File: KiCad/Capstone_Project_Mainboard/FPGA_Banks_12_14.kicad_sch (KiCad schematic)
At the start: 2 parts, among them U1 XC7K160T-FFG676_MIB

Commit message: Updated FPGA Footprint
Added die-to-pad length offsets to all pins of the FFG676 package. These values were derived from the delay files provided in Vivado.
+ Other minor bugfixes
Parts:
- U1: footprint Capstone_Library:Xilinx_FFG676_MOD -> Capstone_Library:Xilinx_FFG676_K7_160T
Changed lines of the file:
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@@
   (title_block
     (title "FPGA Banks 12 & 14 I/O")
-    (date "2023-12-18")
+    (date "2023-12-22")
     (rev "A")
     (company "Jordan Harris-Toovy")
@@
       (effects (font (size 1.27 1.27)) (justify right))
     )
-    (property "Footprint" "Capstone_Library:Xilinx_FFG676_MOD" (at 73.66 20.32 0)
+    (property "Footprint" "Capstone_Library:Xilinx_FFG676_K7_160T" (at 73.66 20.32 0)
       (effects (font (size 1.27 1.27)) hide)
     )
@@
       (effects (font (size 1.27 1.27)) (justify right))
     )
-    (property "Footprint" "Capstone_Library:Xilinx_FFG676_MOD" (at 185.42 20.32 0)
-      (effects (font (size 1.27 1.27)) hide)
-    )
+    (property "Footprint" "Capstone_Library:Xilinx_FFG676_K7_160T" (at 185.42 20.32 0)
+      (effects (font (size 1.27 1.27)) hide)
+    )

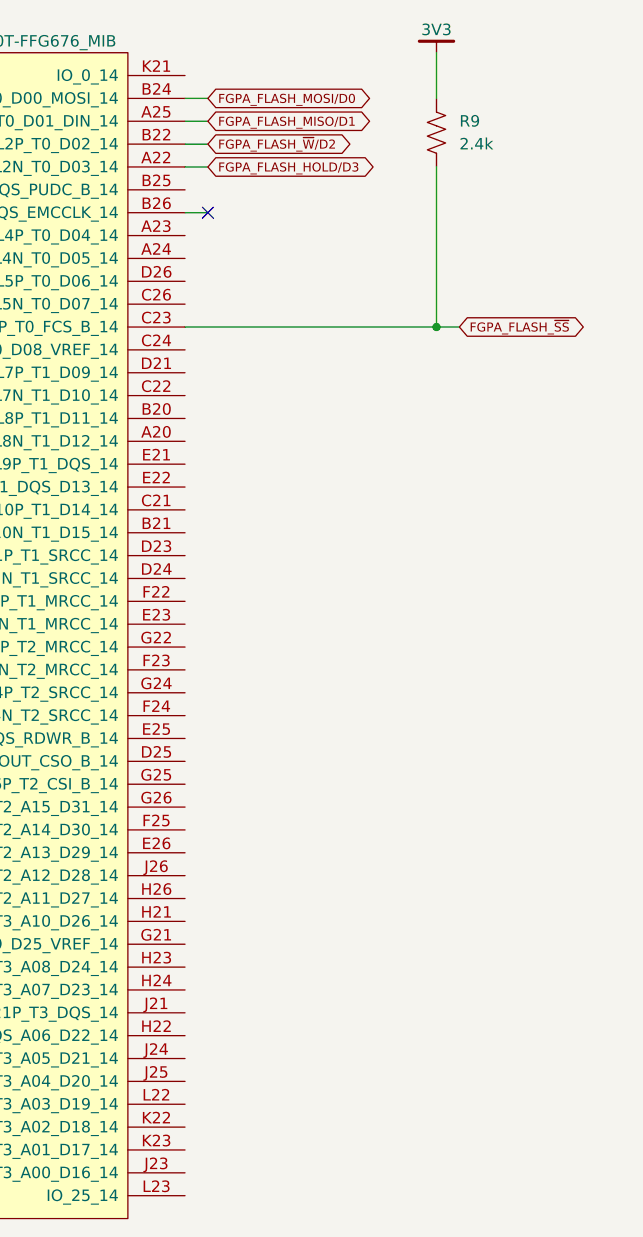
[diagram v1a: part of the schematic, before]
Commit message: Core non-power parts defined
Most major non-power components added to KiCad project
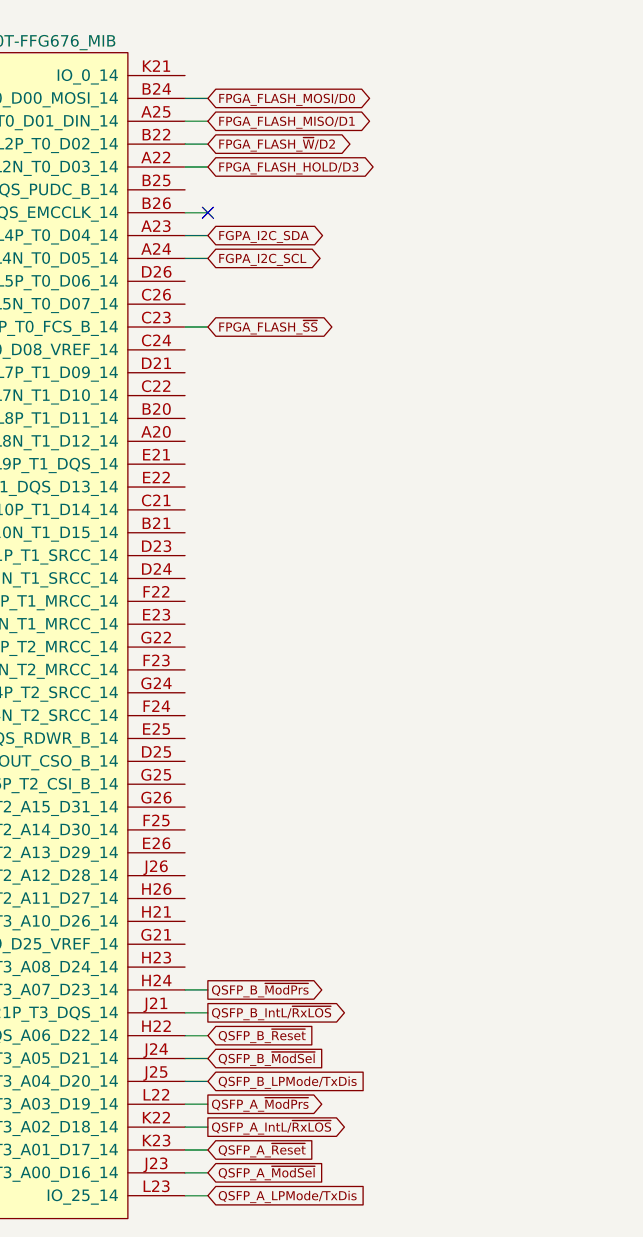
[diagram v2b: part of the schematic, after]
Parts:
- removed R9: 2.4k, symbol Device:R_US
- U1: Part Number (none) -> XC7K160T-2FFG676I
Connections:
- net FGPA_I2C_SDA: now reaches U1.A23 (IO_L4P_T0_D04_14)
- net FGPA_I2C_SCL: now reaches U1.A24 (IO_L4N_T0_D05_14)
- net QSFP_B_~{Reset}: now reaches U1.H22 (IO_L21N_T3_DQS_A06_D22_14)
- net QSFP_B_~{ModPrs}: now reaches U1.H24 (IO_L20N_T3_A07_D23_14)
- net QSFP_B_IntL/~{RxLOS}: now reaches U1.J21 (IO_L21P_T3_DQS_14)
- net QSFP_A_~{ModSel}: now reaches U1.J23 (IO_L24N_T3_A00_D16_14)
- net QSFP_B_~{ModSel}: now reaches U1.J24 (IO_L22P_T3_A05_D21_14)
- net QSFP_B_LPMode/TxDis: now reaches U1.J25 (IO_L22N_T3_A04_D20_14)
- net QSFP_A_IntL/~{RxLOS}: now reaches U1.K22 (IO_L23N_T3_A02_D18_14)
- net QSFP_A_~{Reset}: now reaches U1.K23 (IO_L24P_T3_A01_D17_14)
- net QSFP_A_~{ModPrs}: now reaches U1.L22 (IO_L23P_T3_A03_D19_14)
- net QSFP_A_LPMode/TxDis: now reaches U1.L23 (IO_25_14)
- net FGPA_FLASH_HOLD/D3 renamed FPGA_FLASH_HOLD/D3
- net FGPA_FLASH_MISO/D1 renamed FPGA_FLASH_MISO/D1
- net FGPA_FLASH_MOSI/D0 renamed FPGA_FLASH_MOSI/D0
- net FGPA_FLASH_~{SS} renamed FPGA_FLASH_~{SS}
- net FGPA_FLASH_~{W}/D2 renamed FPGA_FLASH_~{W}/D2
